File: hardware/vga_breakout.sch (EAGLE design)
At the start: 11 parts, among them J1 VGA_DB25, J2 HEADER_5P

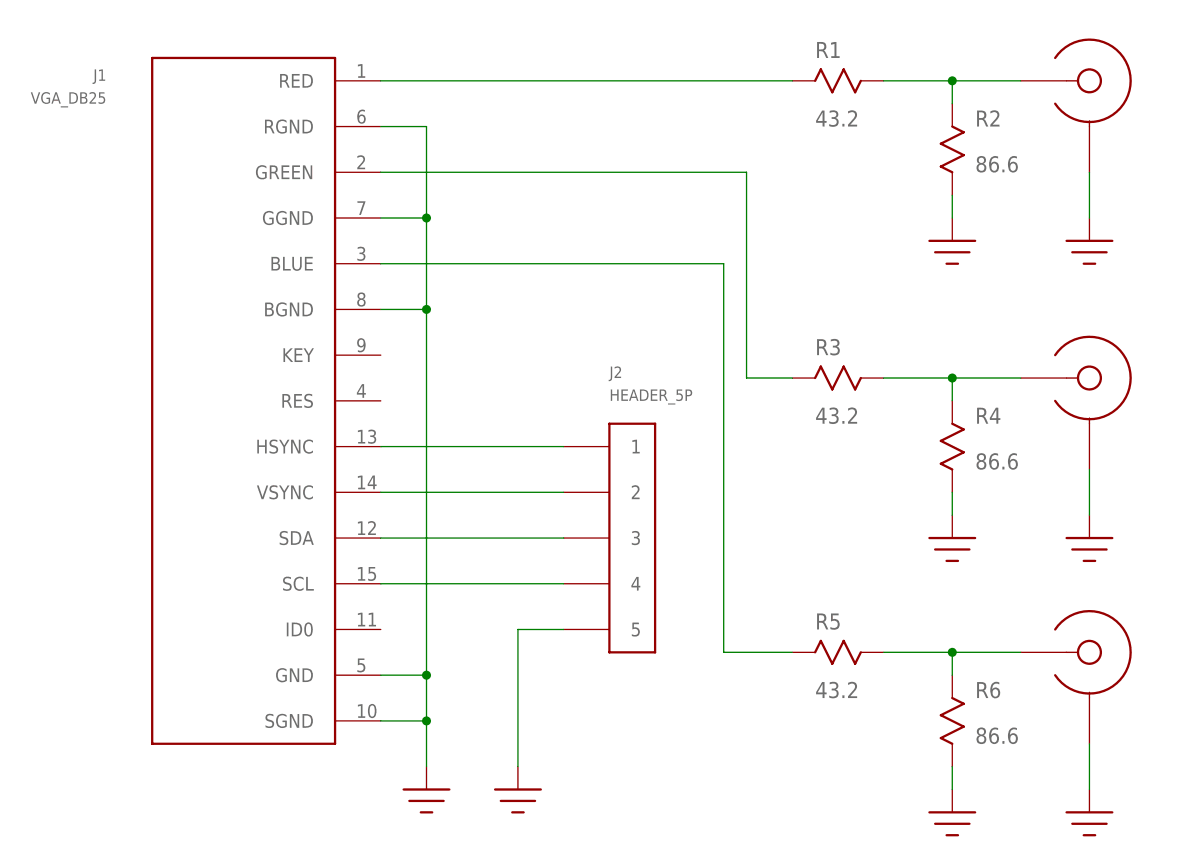
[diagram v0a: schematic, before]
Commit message: added PTH for VGA connector tabs; LPF has SMA jack
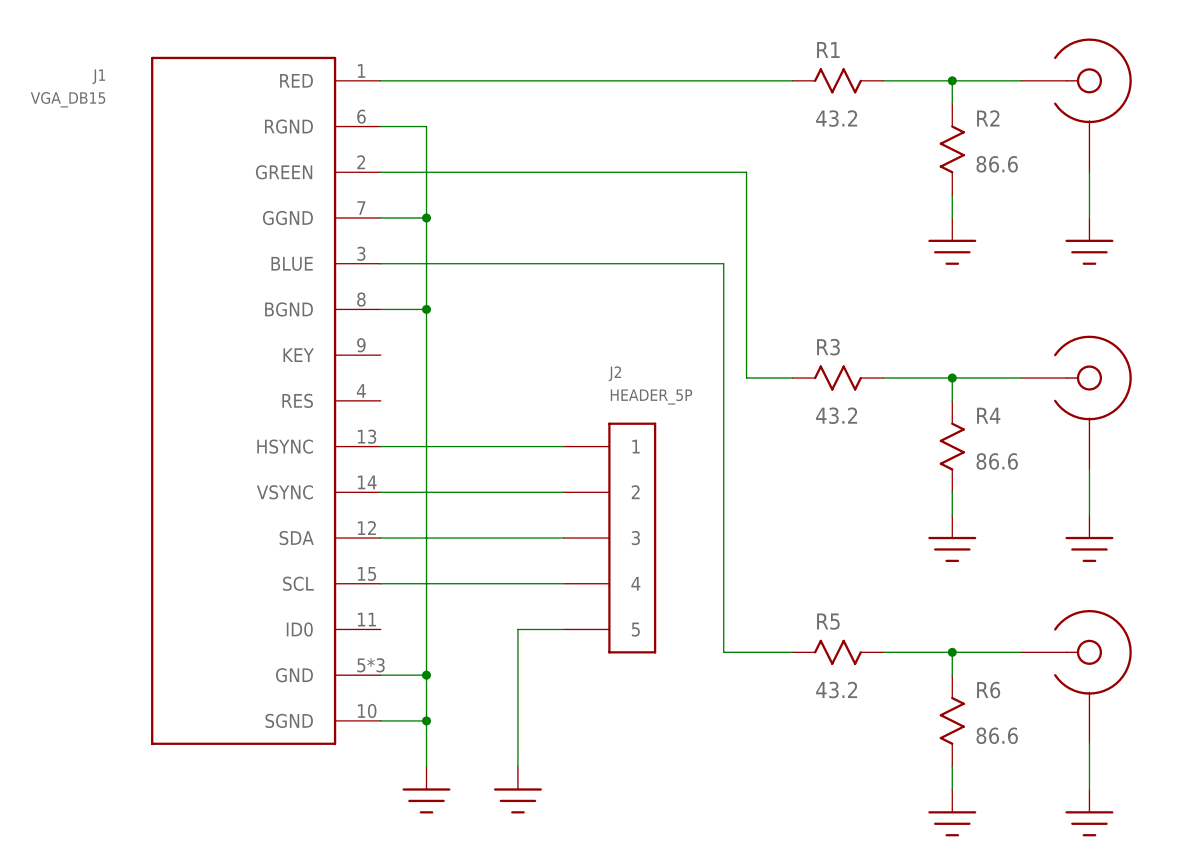
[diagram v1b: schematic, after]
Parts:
- J1: value VGA_DB25 -> VGA_DB15; device mw-voice-marker:VGA_DB25 -> mw-voice-marker:VGA_DB15
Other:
- moved on the sheet: J1
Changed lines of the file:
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@@
 <class number="0" name="default" width="0" drill="0">
+</class>
+<class number="1" name="50ohm" width="1.0414" drill="0">
+<clearance class="1" value="0.2032"/>
+</class>
+<class number="2" name="75ohm" width="0.2032" drill="0">
+<clearance class="2" value="0.1524"/>
 </class>
 </classes>
 <parts>
-<part name="J1" library="mw-voice-marker" deviceset="VGA_DB25" device=""/>
+<part name="J1" library="mw-voice-marker" deviceset="VGA_DB15" device=""/>
 <part name="U$4" library="mw-voice-marker" deviceset="GND" device=""/>
 <part name="U$5" library="mw-voice-marker" deviceset="GND" device=""/>
@@
 </segment>
 </net>
-<net name="N$2" class="0">
+<net name="N$2" class="1">
 <segment>
 <pinref part="R3" gate="G$1" pin="P$3"/>
@@
 </segment>
 </net>
-<net name="N$3" class="0">
+<net name="N$3" class="1">
 <segment>
 <pinref part="U$1" gate="G$1" pin="CENTER"/>
@@
 </segment>
 </net>
-<net name="RED" class="0">
+<net name="RED" class="2">
 <segment>
 <pinref part="R1" gate="G$1" pin="P$3"/>
@@
 </segment>
 </net>
-<net name="GREEN" class="0">
+<net name="GREEN" class="2">
 <segment>
 <pinref part="J1" gate="G$1" pin="GREEN"/>
@@
 </segment>
 </net>
-<net name="BLUE" class="0">
+<net name="BLUE" class="2">
 <segment>
 <pinref part="R5" gate="G$1" pin="P$4"/>

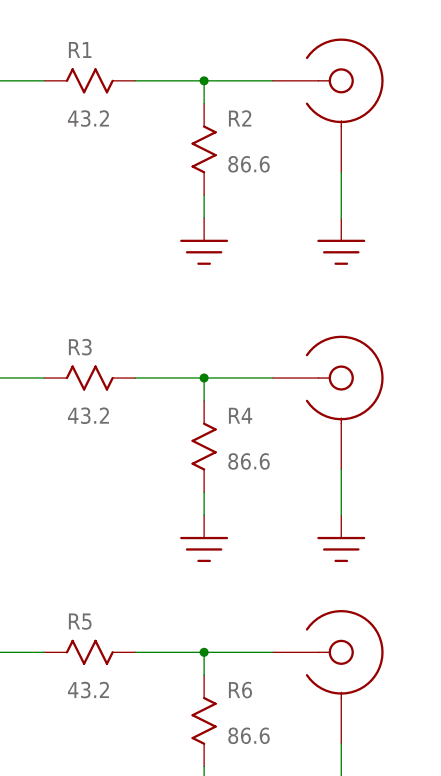
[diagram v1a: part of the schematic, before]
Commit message: updated VGA connector footprint
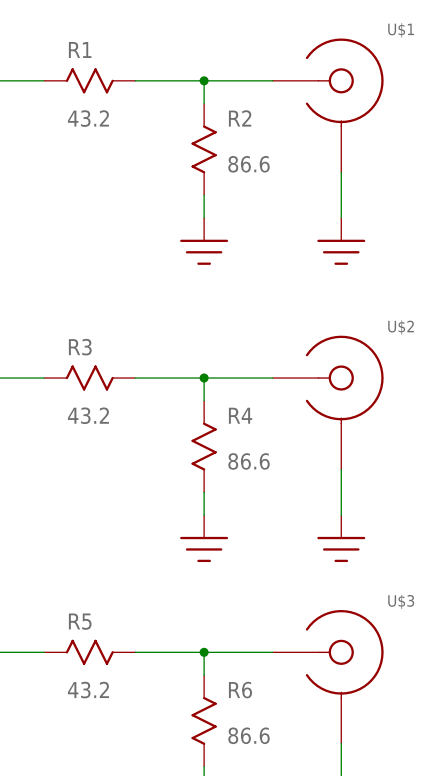
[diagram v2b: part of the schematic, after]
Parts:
- U$1, U$2, U$3: value EDGE_LAUNCH_JACK -> (none)
